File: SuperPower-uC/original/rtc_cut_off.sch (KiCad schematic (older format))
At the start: 17 parts, among them J6 Conn_01x02_Male, Q6 BSS84-7-F, SW1 DNP/SKRKAEE020, U5 RV-3028-C7, U8 TPS70933DRVT

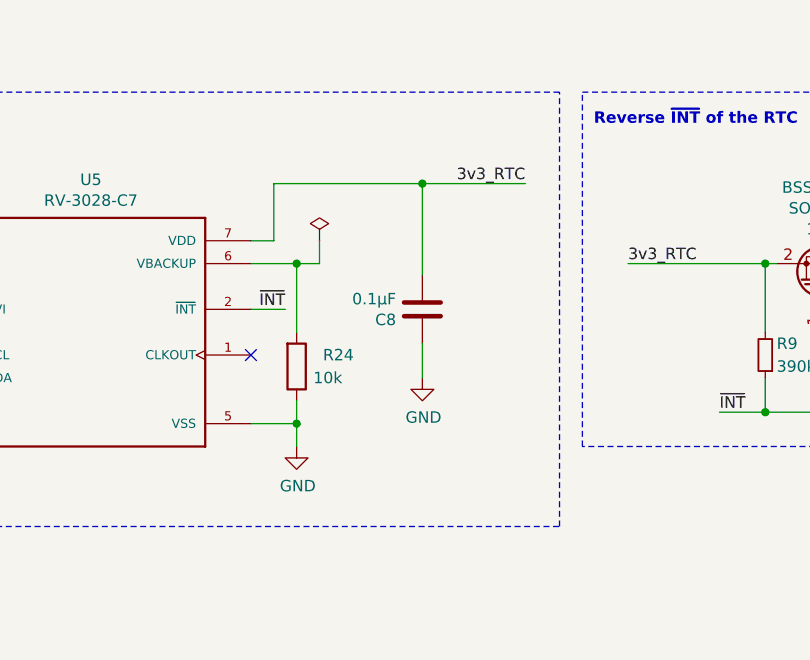
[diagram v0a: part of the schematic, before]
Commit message: Shrink board height + Add Coin cell holder
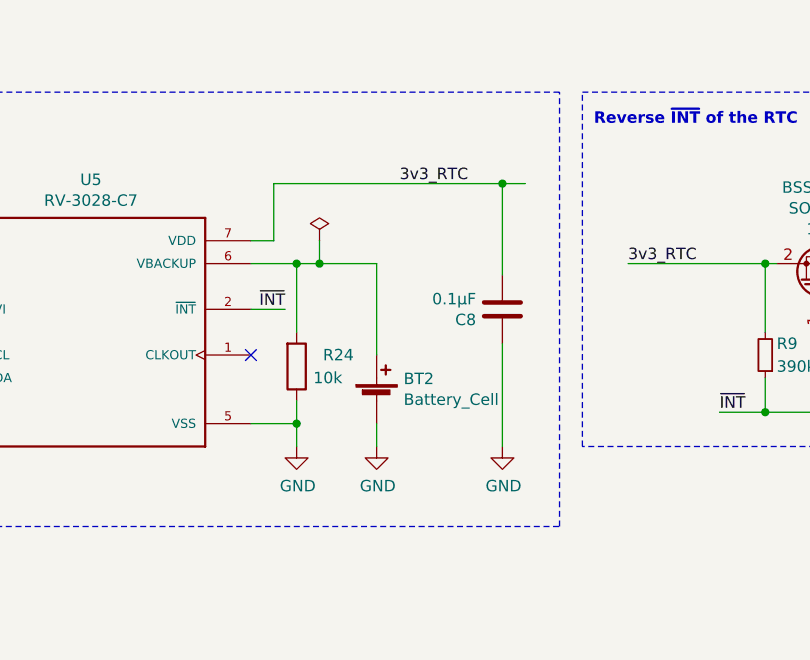
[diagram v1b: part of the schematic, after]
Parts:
- added BT2: Battery_Cell, Battery:BatteryHolder_Keystone_3000_1x12mm, symbol Device:Battery_Cell
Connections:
- net GND: now also BT2.2 (-)
- net at R24.2, U5.6 (VBACKUP): now also BT2.1 (+)
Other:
- moved on the sheet: C8
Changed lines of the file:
@@
 L Device:C C8
 U 1 1 5F716113
-P 6900 4100
-F 0 "C8" H 7015 4146 50  0000 L CNN
-F 1 "0.1µF" H 7015 4055 50  0000 L CNN
-F 2 "Capacitor_SMD:C_0603_1608Metric" H 6938 3950 50  0001 C CNN
-F 3 "~" H 6900 4100 50  0001 C CNN
-	1    6900 4100
+P 7250 4100
+F 0 "C8" H 7365 4146 50  0000 L CNN
+F 1 "0.1µF" H 7365 4055 50  0000 L CNN
+F 2 "Capacitor_SMD:C_0603_1608Metric" H 7288 3950 50  0001 C CNN
+F 3 "~" H 7250 4100 50  0001 C CNN
+	1    7250 4100
 	-1   0    0    1
 $EndComp
 Wire Wire Line
-	6900 3950 6900 3550
+	7250 3950 7250 3550
 Text Label 6300 4100 2    50   ~ 0
 ~INT
@@
 L power:GND #PWR041
 U 1 1 5FBD2731
-P 6900 4400
-F 0 "#PWR041" H 6900 4150 50  0001 C CNN
-F 1 "GND" H 6905 4227 50  0000 C CNN
-F 2 "" H 6900 4400 50  0001 C CNN
-F 3 "" H 6900 4400 50  0001 C CNN
-	1    6900 4400
-	1    0    0    -1
-$EndComp
-Wire Wire Line
-	6900 4250 6900 4400
+P 7250 4700
+F 0 "#PWR041" H 7250 4450 50  0001 C CNN
+F 1 "GND" H 7255 4527 50  0000 C CNN
+F 2 "" H 7250 4700 50  0001 C CNN
+F 3 "" H 7250 4700 50  0001 C CNN
+	1    7250 4700
+	1    0    0    -1
+$EndComp
+Wire Wire Line
+	7250 4250 7250 4700
 Wire Wire Line
 	6250 3800 6150 3800
@@
 Wire Notes Line
 	550  550  550  1850
-Text Label 7350 3550 2    50   ~ 0
-3v3_RTC
-Wire Wire Line
-	7350 3550 6900 3550
+Text Label 7100 3550 2    50   ~ 0
+3v3_RTC
+Wire Wire Line
+	7350 3550 7250 3550
 Wire Wire Line
 	6250 3550 6250 3800
 Wire Wire Line
 	6300 4100 6150 4100
-Wire Wire Line
-	6900 3550 6250 3550
-Connection ~ 6900 3550
 Wire Wire Line
 	1350 6350 1500 6350
@@
 Text Notes 7650 3300 0    50   ~ 10
 Reverse ~INT~ of the RTC
+$Comp
+L Device:Battery_Cell BT2
+U 1 1 5FE2495F
+P 6700 4500
+F 0 "BT2" H 6818 4596 50  0000 L CNN
+F 1 "Battery_Cell" H 6818 4505 50  0000 L CNN
+F 2 "Battery:BatteryHolder_Keystone_3000_1x12mm" V 6700 4560 50  0001 C CNN
+F 3 "~" V 6700 4560 50  0001 C CNN
+	1    6700 4500
+	1    0    0    -1
+$EndComp
+$Comp
+L power:GND #PWR0108
+U 1 1 5FE25662
+P 6700 4700
+F 0 "#PWR0108" H 6700 4450 50  0001 C CNN
+F 1 "GND" H 6705 4527 50  0000 C CNN
+F 2 "" H 6700 4700 50  0001 C CNN
+F 3 "" H 6700 4700 50  0001 C CNN
+	1    6700 4700
+	1    0    0    -1
+$EndComp
+Wire Wire Line
+	6700 4600 6700 4700
+Connection ~ 7250 3550
+Wire Wire Line
+	6250 3550 7250 3550
+Wire Wire Line
+	6700 4300 6700 3900
+Wire Wire Line
+	6700 3900 6450 3900
+Connection ~ 6450 3900
 $EndSCHEMATC

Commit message: Update Single rows Headers to be fully compatible with ESP WROOM modules
(ESP-32 DevKit C rev. 4)
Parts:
- J6: footprint Connector_PinSocket_2.54mm:PinSocket_1x02_P2.54mm_Vertical -> Connector_PinHeader_2.54mm:PinHeader_1x02_P2.54mm_Vertical
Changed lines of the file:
@@
 F 0 "J6" H 4250 2350 50  0000 C CNN
 F 1 "Conn_01x02_Male" H 4000 2250 50  0000 C CNN
-F 2 "Connector_PinSocket_2.54mm:PinSocket_1x02_P2.54mm_Vertical" H 4350 2300 50  0001 C CNN
+F 2 "Connector_PinHeader_2.54mm:PinHeader_1x02_P2.54mm_Vertical" H 4350 2300 50  0001 C CNN
 F 3 "~" H 4350 2300 50  0001 C CNN
 	1    4350 2300
